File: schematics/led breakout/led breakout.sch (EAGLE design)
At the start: 3 parts

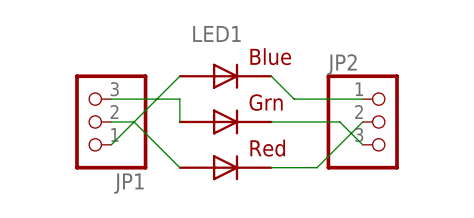
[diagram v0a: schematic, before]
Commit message: Had wrong pin headers (too small), but worked out since the difference is not that big and there are only 3 pins on each side.
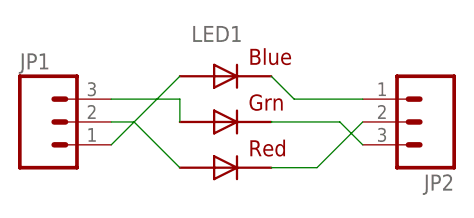
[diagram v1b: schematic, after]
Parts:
- JP1, JP2: device pinhead:PINHD-1X3 -> SparkFun-Connectors:M03PTH
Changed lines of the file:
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@@
 <layer number="97" name="Info" color="7" fill="1" visible="yes" active="yes"/>
 <layer number="98" name="Guide" color="6" fill="1" visible="yes" active="yes"/>
+<layer number="99" name="SpiceOrder" color="7" fill="1" visible="yes" active="yes"/>
 <layer number="100" name="Muster" color="7" fill="1" visible="no" active="no"/>
 <layer number="101" name="Patch_Top" color="12" fill="4" visible="yes" active="yes"/>
@@
 <layer number="111" name="LPC17xx" color="7" fill="1" visible="yes" active="yes"/>
 <layer number="112" name="tSilk" color="7" fill="1" visible="yes" active="yes"/>
+<layer number="113" name="IDFDebug" color="4" fill="1" visible="yes" active="yes"/>
 <layer number="116" name="Patch_BOT" color="9" fill="4" visible="yes" active="yes"/>
 <layer number="121" name="_tsilk" color="7" fill="1" visible="yes" active="yes"/>
@@
 <parts>
 <part name="LED1" library="adafruit" deviceset="RGBLED" device="5050"/>
-<part name="JP1" library="pinhead" deviceset="PINHD-1X3" device=""/>
-<part name="JP2" library="pinhead" deviceset="PINHD-1X3" device=""/>
+<part name="JP1" library="SparkFun-Connectors" deviceset="M03" device="PTH"/>
+<part name="JP2" library="SparkFun-Connectors" deviceset="M03" device="PTH"/>
 </parts>
 <sheets>
@@
 <instances>
 <instance part="LED1" gate="G$1" x="35.56" y="40.64"/>
-<instance part="JP1" gate="A" x="20.32" y="40.64" rot="R180"/>
-<instance part="JP2" gate="A" x="53.34" y="40.64"/>
+<instance part="JP1" gate="G$1" x="15.24" y="40.64"/>
+<instance part="JP2" gate="G$1" x="58.42" y="40.64" rot="R180"/>
 </instances>
 <busses>
@@
 <net name="N$4" class="0">
 <segment>
-<pinref part="JP2" gate="A" pin="1"/>
 <pinref part="LED1" gate="G$1" pin="BLUE_C"/>
 <wire x1="50.8" y1="43.18" x2="43.18" y2="43.18" width="0.1524" layer="91"/>
 <wire x1="43.18" y1="43.18" x2="40.64" y2="45.72" width="0.1524" layer="91"/>
+<pinref part="JP2" gate="G$1" pin="1"/>
 </segment>
 </net>
 <net name="N$1" class="0">
 <segment>
-<pinref part="JP1" gate="A" pin="3"/>
 <pinref part="LED1" gate="G$1" pin="GREEN_A"/>
 <wire x1="22.86" y1="43.18" x2="30.48" y2="43.18" width="0.1524" layer="91"/>
 <wire x1="30.48" y1="43.18" x2="30.48" y2="40.64" width="0.1524" layer="91"/>
+<pinref part="JP1" gate="G$1" pin="3"/>
 </segment>
 </net>
 <net name="N$2" class="0">
 <segment>
-<pinref part="JP1" gate="A" pin="2"/>
 <pinref part="LED1" gate="G$1" pin="RED_A"/>
 <wire x1="22.86" y1="40.64" x2="25.4" y2="40.64" width="0.1524" layer="91"/>
 <wire x1="25.4" y1="40.64" x2="30.48" y2="35.56" width="0.1524" layer="91"/>
+<pinref part="JP1" gate="G$1" pin="2"/>
 </segment>
 </net>
 <net name="N$3" class="0">
 <segment>
-<pinref part="JP1" gate="A" pin="1"/>
 <pinref part="LED1" gate="G$1" pin="BLUE_A"/>
 <wire x1="22.86" y1="38.1" x2="30.48" y2="45.72" width="0.1524" layer="91"/>
+<pinref part="JP1" gate="G$1" pin="1"/>
 </segment>
 </net>
@@
 <segment>
 <pinref part="LED1" gate="G$1" pin="RED_C"/>
-<pinref part="JP2" gate="A" pin="2"/>
 <wire x1="40.64" y1="35.56" x2="45.72" y2="35.56" width="0.1524" layer="91"/>
 <wire x1="45.72" y1="35.56" x2="50.8" y2="40.64" width="0.1524" layer="91"/>
+<pinref part="JP2" gate="G$1" pin="2"/>
 </segment>
 </net>
@@
 <segment>
 <pinref part="LED1" gate="G$1" pin="GREEN_C"/>
-<pinref part="JP2" gate="A" pin="3"/>
 <wire x1="40.64" y1="40.64" x2="48.26" y2="40.64" width="0.1524" layer="91"/>
 <wire x1="48.26" y1="40.64" x2="50.8" y2="38.1" width="0.1524" layer="91"/>
+<pinref part="JP2" gate="G$1" pin="3"/>
 </segment>
 </net>
